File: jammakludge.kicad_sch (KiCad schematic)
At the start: 3 parts

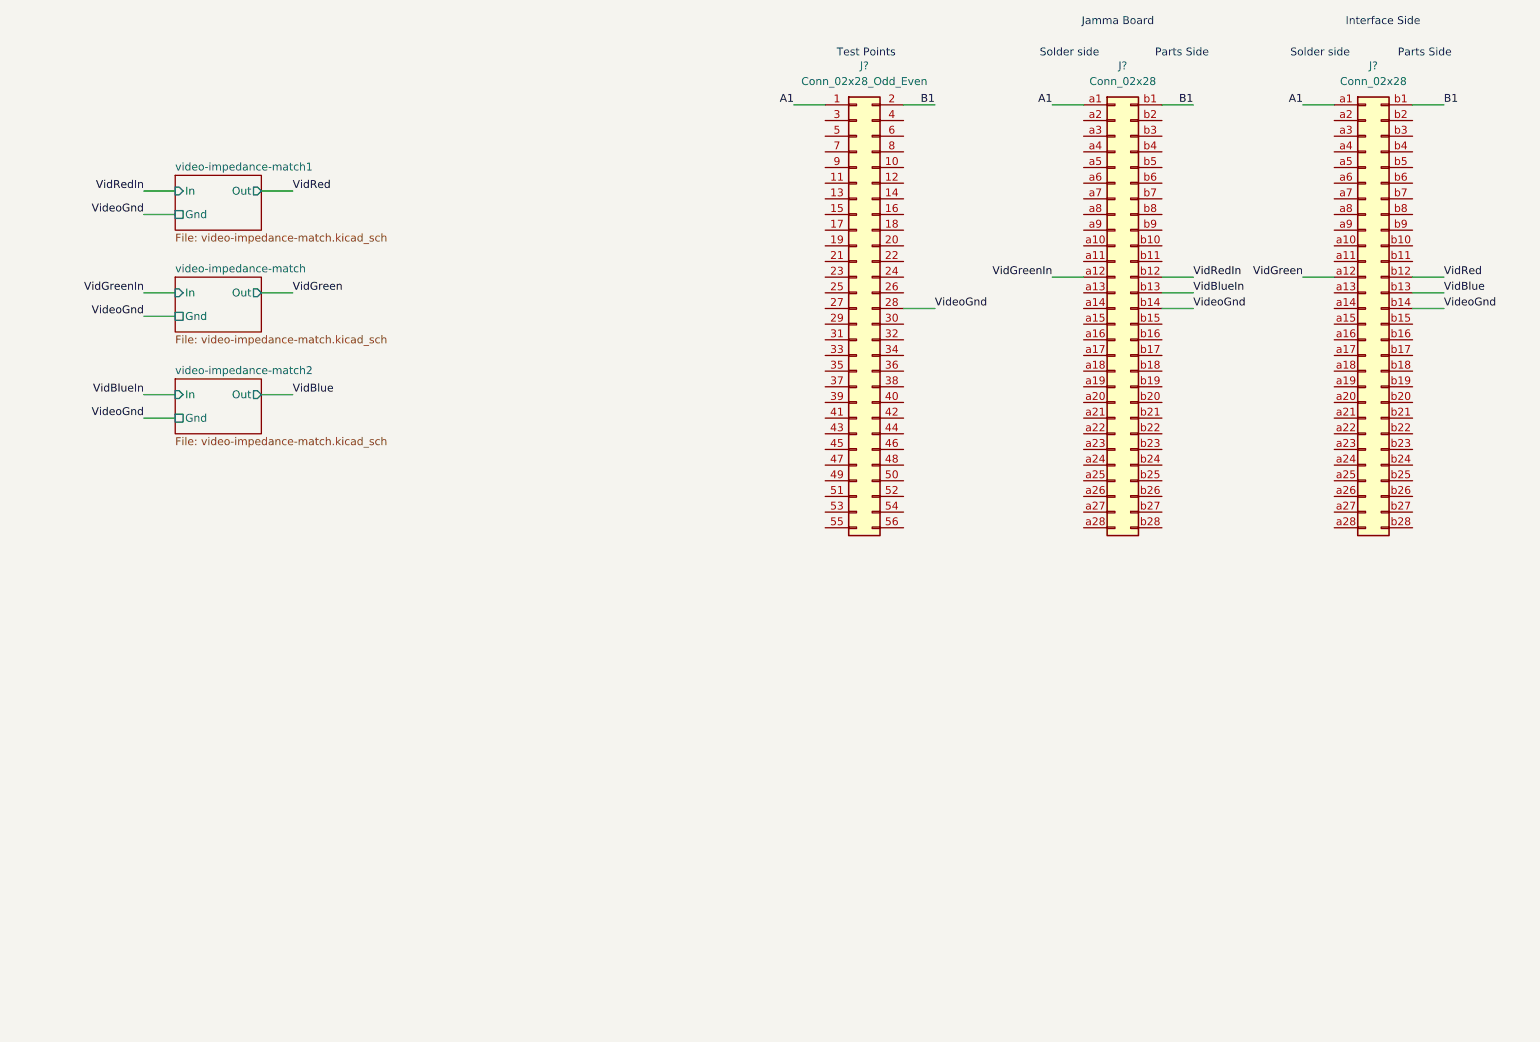
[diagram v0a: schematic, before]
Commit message: Jamma symbol and footprint added. Power supply caps added to schematic.
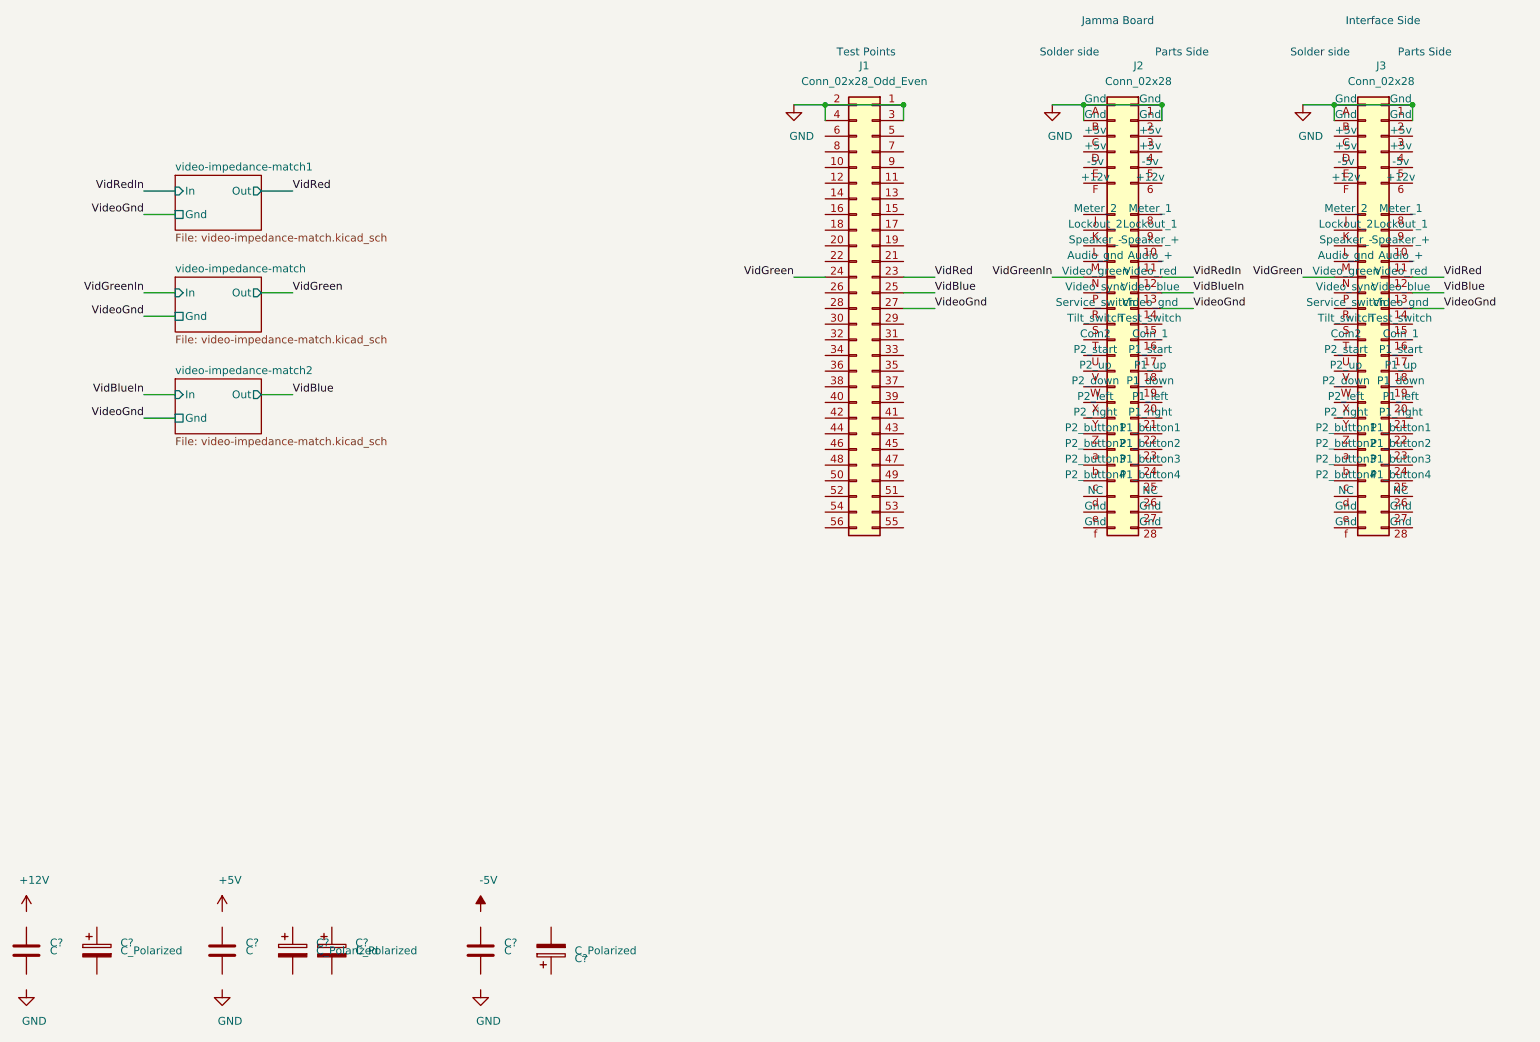
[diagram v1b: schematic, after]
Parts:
- added C? (x4): C_Polarized, symbol Device:C_Polarized
- added C? (x3): C, symbol Device:C
- J2: renamed from J?; symbol Connector_Generic:Conn_02x28_Row_Letter_First -> jamma:jamma
- J3: renamed from J?; footprint (none) -> jamma:JAMMA-56; symbol Connector_Generic:Conn_02x28_Row_Letter_First -> jamma:jamma
- gave numbers to parts that had none: 1
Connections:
- net VidBlue: now also J1.25 (Pin_25), J3.13 (Video_blue); no longer J3.b13 (Pin_b13)
- net VidBlueIn: now also J2.13 (Video_blue); no longer J2.b13 (Pin_b13)
- net VidGreen: now also J1.24 (Pin_24), J3.N (Video_green); no longer J3.a12 (Pin_a12)
- net VidGreenIn: now also J2.N (Video_green); no longer J2.a12 (Pin_a12)
- net VidRed: now also J1.23 (Pin_23), J3.12 (Video_red); no longer J3.b12 (Pin_b12)
- net VidRedIn: now also J2.12 (Video_red); no longer J2.b12 (Pin_b12)
- net VideoGnd: now also J1.27 (Pin_27), J2.14 (Video_gnd), J3.14 (Video_gnd); no longer J1.28 (Pin_28), J2.b14 (Pin_b14), J3.b14 (Pin_b14)
- net GND: now reaches J1.3 (Pin_3)
- net GND: now also J1.1 (Pin_1), J1.2 (Pin_2), J1.4 (Pin_4), J2.1 (Gnd), J2.2 (Gnd), J2.A (Gnd), J2.B (Gnd), J3.1 (Gnd), J3.2 (Gnd), J3.A (Gnd), J3.B (Gnd)
- removed net A1: J1.1 (Pin_1), J2.a1 (Pin_a1), J3.a1 (Pin_a1)
- removed net B1: J1.2 (Pin_2), J2.b1 (Pin_b1), J3.b1 (Pin_b1)

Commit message: Progress with labels and footprints
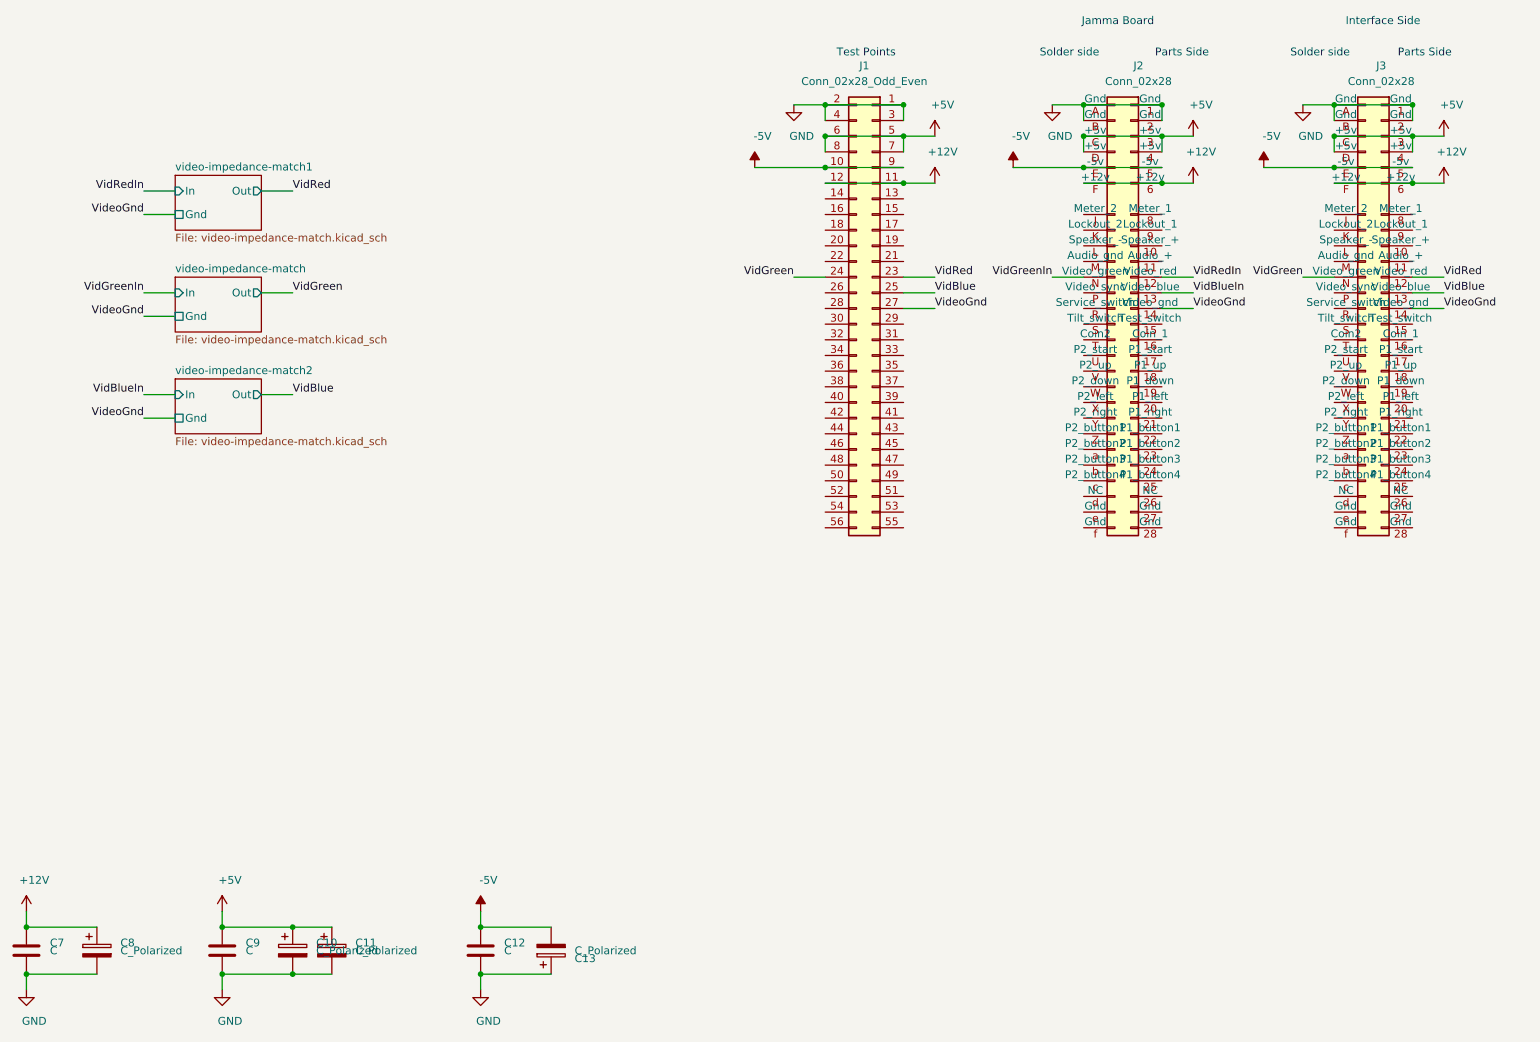
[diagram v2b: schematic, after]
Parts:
- C10, C13, C8: renamed from C?; footprint (none) -> Capacitor_THT:CP_Radial_D5.0mm_P2.00mm
- C11: renamed from C?; footprint (none) -> Capacitor_THT:CP_Radial_D6.3mm_P2.50mm
- C12, C7, C9: renamed from C?; footprint (none) -> Capacitor_SMD:C_0603_1608Metric
- J1: footprint (none) -> Connector_PinHeader_2.54mm:PinHeader_2x28_P2.54mm_Vertical
- J2: footprint (none) -> jamma:JAMMA-56
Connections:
- net +12V: now also C7.1, C8.1, J1.11 (Pin_11), J1.12 (Pin_12), J2.6 (+12v), J2.F (+12v), J3.6 (+12v), J3.F (+12v)
- net +5V: now also C10.1, C11.1, C9.1, J1.5 (Pin_5), J1.6 (Pin_6), J1.7 (Pin_7), J1.8 (Pin_8), J2.3 (+5v), J2.4 (+5v), J2.C (+5v), J2.D (+5v), J3.3 (+5v), J3.4 (+5v), J3.C (+5v), J3.D (+5v)
- net -5V: now also C12.1, C13.2, J1.10 (Pin_10), J1.9 (Pin_9), J2.5 (-5v), J2.E (-5v), J3.5 (-5v), J3.E (-5v)
- net GND: now also C10.2, C11.2, C12.2, C13.1, C7.2, C8.2, C9.2

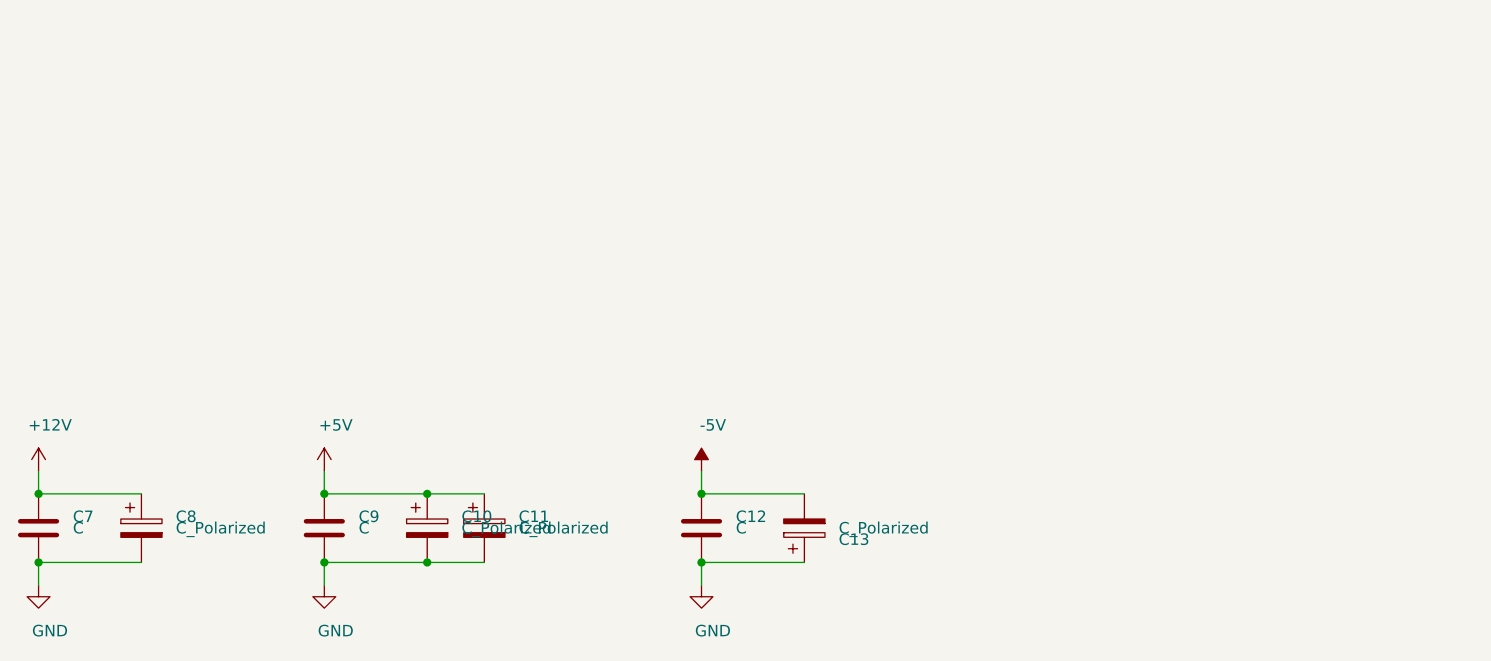
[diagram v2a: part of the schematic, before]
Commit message: Added more power bypassing capacitors to 5v and 12v supplies.
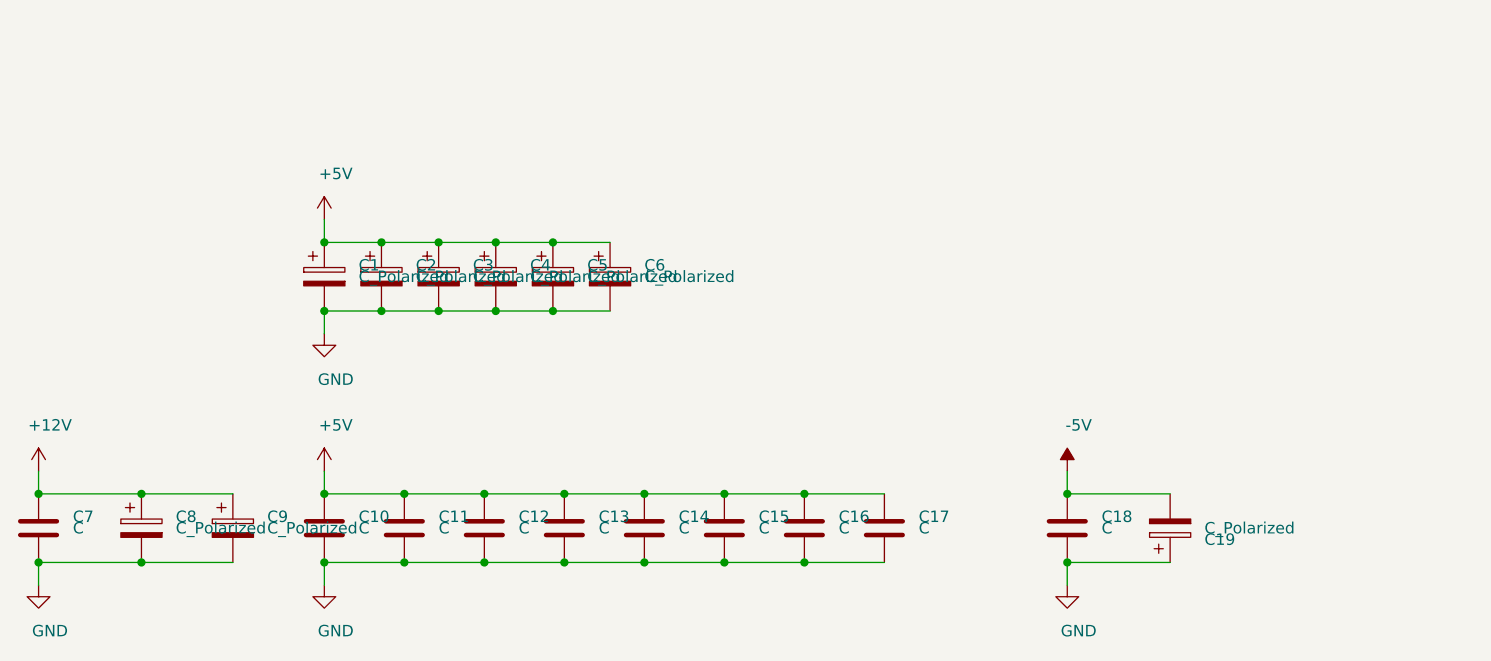
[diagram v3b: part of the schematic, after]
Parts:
- added C11, C12, C13: C, Capacitor_SMD:C_0603_1608Metric, symbol Device:C
- added C14, C15, C16, C17: C, Capacitor_SMD:C_0805_2012Metric, symbol Device:C
- added C3: C_Polarized, Capacitor_THT:CP_Radial_D5.0mm_P2.50mm, symbol Device:C_Polarized
- added C4: C_Polarized, Capacitor_THT:CP_Radial_D8.0mm_P3.50mm, symbol Device:C_Polarized
- added C5, C6, C9: C_Polarized, Capacitor_THT:CP_Radial_D10.0mm_P5.00mm, symbol Device:C_Polarized
- C1: renamed from C10; footprint Capacitor_THT:CP_Radial_D5.0mm_P2.00mm -> Capacitor_THT:CP_Radial_D5.0mm_P2.50mm
- C19: renamed from C13; footprint Capacitor_THT:CP_Radial_D5.0mm_P2.00mm -> Capacitor_THT:CP_Radial_D5.0mm_P2.50mm
- C2: renamed from C11; footprint Capacitor_THT:CP_Radial_D6.3mm_P2.50mm -> Capacitor_THT:CP_Radial_D8.0mm_P3.50mm
- C8: footprint Capacitor_THT:CP_Radial_D5.0mm_P2.00mm -> Capacitor_THT:CP_Radial_D5.0mm_P2.50mm
- renumbered C9 to C10, C12 to C18
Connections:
- net +12V: now also C9.1
- net +5V: now also C11.1, C12.1, C13.1, C14.1, C15.1, C16.1, C17.1, C3.1, C4.1, C5.1, C6.1
- net GND: now also C11.2, C12.2, C13.2, C14.2, C15.2, C16.2, C17.2, C3.2, C4.2, C5.2, C6.2, C9.2
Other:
- moved on the sheet: C1, C18, C19, C2
